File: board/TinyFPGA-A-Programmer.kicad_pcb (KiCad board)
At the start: 2 copper layers, 17.8 x 30.5 mm, 17 parts, among them J1 USB, J2 JTAG, J3 ICSP, J4 CONN_01X06, U1 PIC16F1455-QFN16, U2 MIC5504-3.3YM5-TR

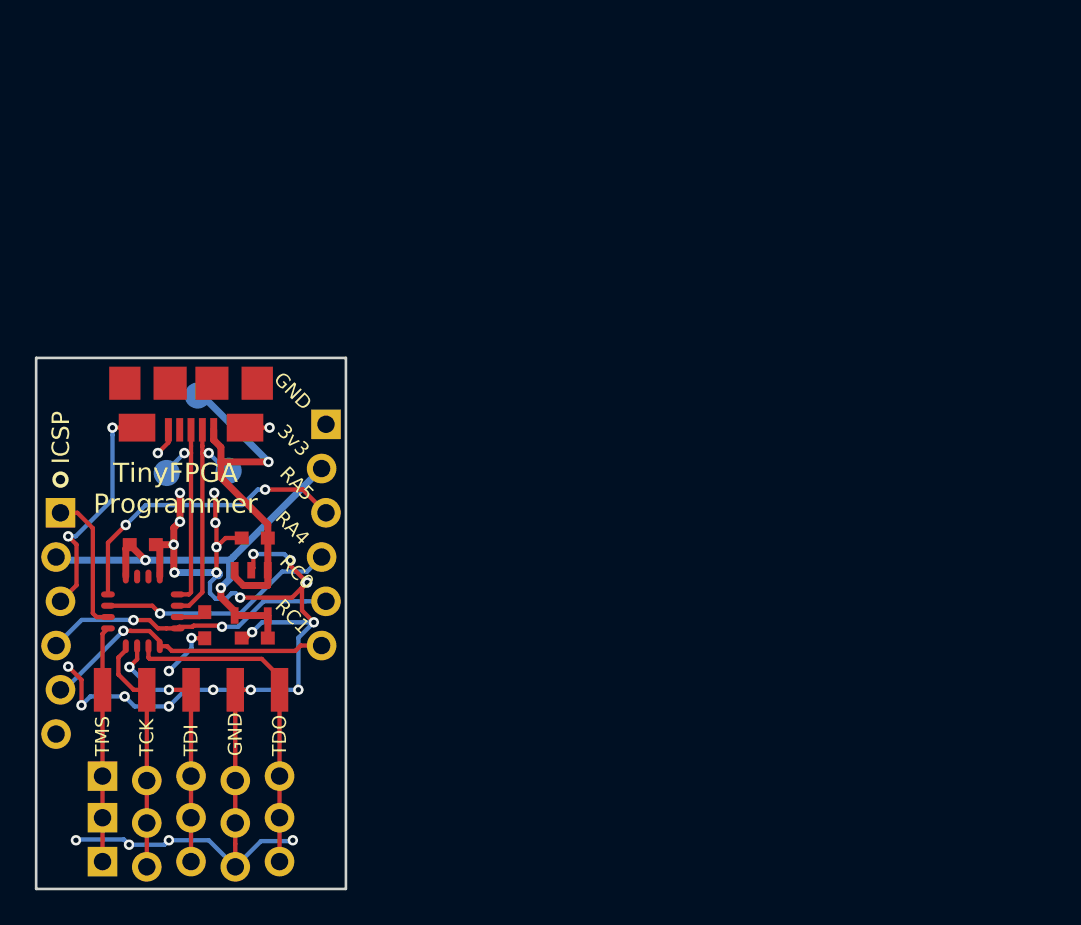
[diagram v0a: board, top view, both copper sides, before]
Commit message: Change PIC footprint and shape
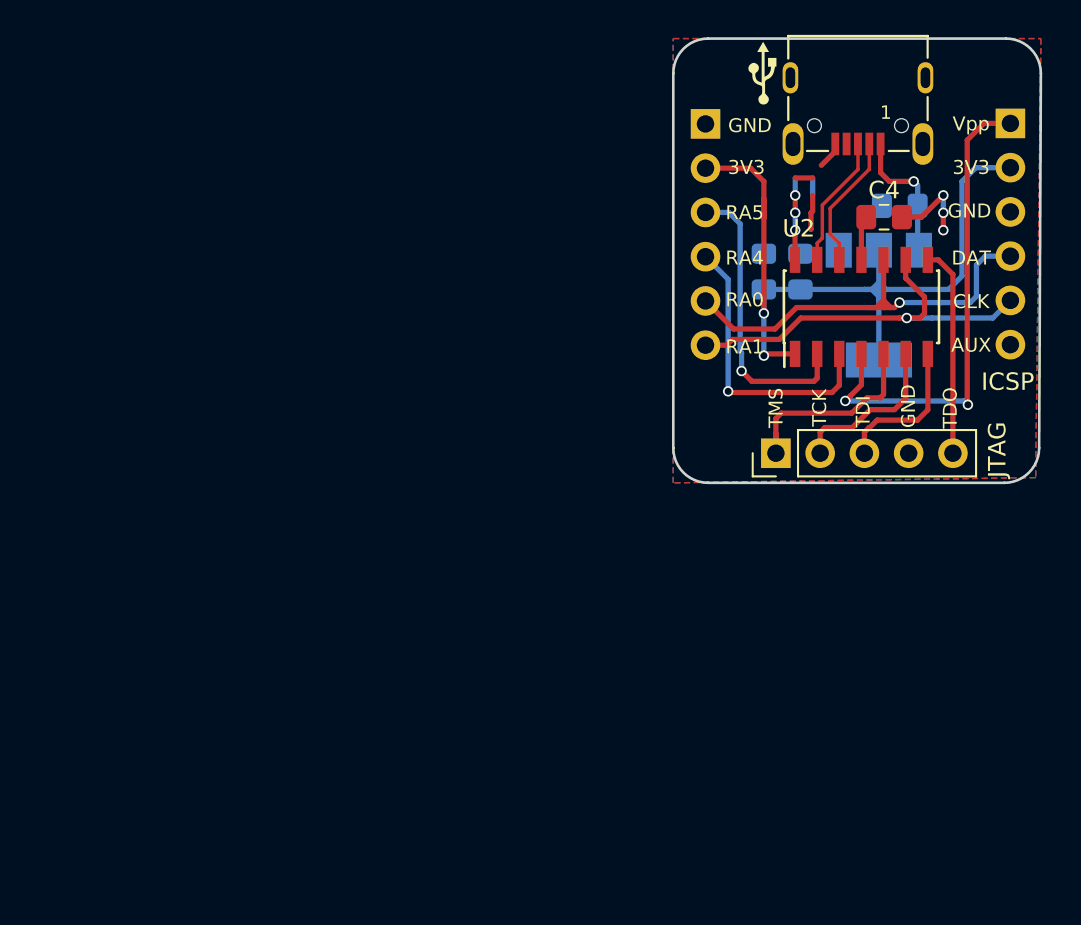
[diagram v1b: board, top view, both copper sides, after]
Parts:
- removed D+, D-, VUSB: TEST, Measurement_Points:Measurement_Point_Round-SMD-Pad_Small
- removed the J2 at (147.3, 119.4)
- removed the J2 at (142.2, 124.5)
- removed the J2 at (142.2, 126.9)
- removed the J2 at (142.2, 129.4)
- removed REF***: OSHW-Logo_5.7x6mm_SilkScreen, Symbols:OSHW-Logo_5.7x6mm_SilkScreen
- added J2: JTAG, Connector_PinHeader_2.54mm:PinHeader_1x05_P2.54mm_Vertical, F.Cu at (180.9, 105.8)
- added REF**: OSHW-Logo2_7.3x6mm_SilkScreen, Symbol:OSHW-Logo2_7.3x6mm_SilkScreen, B.Cu at (185.5, 84.9)
- added svg2mod: G***, Aesthetics:usb_graphic, F.Cu at (180.1, 84.0)
- C1, C2, C3: footprint Capacitors_SMD:C_0603 -> Capacitor_SMD:C_0805_2012Metric_Pad1.15x1.40mm_HandSolder; moved to B.Cu
- C4: footprint Capacitors_SMD:C_0603 -> Capacitor_SMD:C_0805_2012Metric_Pad1.15x1.40mm_HandSolder
- J1: footprint TinyFPGA:FCI-Micro-USB -> Connectors:629105150521
- J3, J4: footprint Pin_Headers:Pin_Header_Straight_1x06_Pitch2.54mm -> Connector_PinHeader_2.54mm:PinHeader_1x06_P2.54mm_Vertical; moved to B.Cu
- U1: value PIC16F1455-QFN16 -> AP1117-33; footprint Housings_DFN_QFN:QFN-16-1EP_4x4mm_Pitch0.65mm -> Package_TO_SOT_SMD:SOT-223-3_TabPin2; moved to B.Cu
- U2: value MIC5504-3.3YM5-TR -> PIC16F1455-ISL; footprint TinyFPGA:SOT23 -> Package_SO:SOIC-14_3.9x8.7mm_P1.27mm
- moved J3 59.0 mm to (194.3, 86.9), turned to 180 degrees
- moved U1 45.8 mm to (186.8, 97.3), turned to 270 degrees
- moved C4 45.5 mm to (187.1, 92.2), turned to 180 degrees
- moved C1 41.6 mm to (188.0, 91.6)
- moved J1 41.0 mm to (185.6, 87.0)
- moved C3 38.9 mm to (180.2, 95.4), turned to 90 degrees
- moved U2 38.7 mm to (185.8, 97.4), turned to 90 degrees
- moved C2 37.7 mm to (182.3, 95.4), turned to 90 degrees
- moved J4 27.9 mm to (176.8, 86.9), turned to 180 degrees
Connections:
- J1 pad 2: Net-(J1-Pad2) -> /D-
- J1 pad 3: Net-(J1-Pad3) -> /D+
- U1 pad 1: RA5 -> GND
- U1 pad 2: RA4 -> +3V3
- U1 pad 3: VPP -> +5V
- U2 pad 1: +5V -> +3V3
- U2 pad 2: GND -> RA5
- U2 pad 3: +5V -> RA4
- U2 pad 4: +3V3 -> VPP
- U2 pad 5: +3V3 -> /RC5
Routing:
- net GND: track 101.2 -> 15.1 mm, vias 31 -> 6
- net +3V3: track 27.7 -> 47.8 mm
- net VPP: track 8.59 -> 28.3 mm, vias 0 -> 2
- net Net-(J2-Pad5): track 19.3 -> 0.00 mm
- net Net-(J2-Pad3): track 15.8 -> 0.00 mm, vias 2 -> 0
- net Net-(J2-Pad2): track 13.9 -> 0.00 mm
- net +5V: track 21.6 -> 7.83 mm
- net Net-(J2-Pad1): track 13.6 -> 0.00 mm
- net Net-(J1-Pad2): track 13.0 -> 0.00 mm, vias 1 -> 0
- net /RC5: track 0.00 -> 12.2 mm
- net Net-(J1-Pad3): track 12.1 -> 0.00 mm, vias 1 -> 0
- net /RC2: track 0.00 -> 12.0 mm
- net /RC4: track 0.00 -> 9.47 mm
- net ICSPDAT: track 17.0 -> 26.0 mm, vias 2 -> 1
- net /RC3: track 0.00 -> 8.59 mm
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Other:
- board size 17.8 x 30.5 mm -> 21.1 x 25.5 mm
- net class Default: clearance 0.2 -> 0.25; trace_width 0.25 -> 0.3
- net class USB added: clearance 0.25, trace_width 0.3, via_dia 0.6, via_drill 0.4
- rule trace_clearance: 0.2 -> 0.25
- board text added: "3V3"
- board text added: "AUX"
- board text added: "CLK"
- board text added: "DAT"
- board text added: "Programmer"
- board text added: "RA0"
- board text added: "RA1"
- board text added: "RC2"
- board text added: "RC3"
- board text added: "RC4"
- board text added: "RC5"
- board text added: "TinyFPGA"
- board text added: "Vpp"
- board text removed: ".125"
- board text removed: ".150"
- board text removed: ".175"
- board text removed: "3v3"
- board text removed: "RC0"
- board text removed: "RC1"
- board text removed: "RC2/TDO"
- board text removed: "RC3/TDI"
- board text removed: "RC4/TCK"
- board text removed: "RC5/TMS"
- board text removed: "TinyFPGA Programmer"
